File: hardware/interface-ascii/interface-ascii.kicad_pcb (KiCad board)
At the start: 2 copper layers, 88.9 x 132.1 mm, 49 parts, among them J1 Apple 2, J2 Apple 1, J3 UART, J4 Conn_01x05, J5 ISP header, J6 Keyboard, J7 SOL-20, SW1 Options, U1 ATmega328P, U2 74LS166, U3 74LS138, U4 74LS138, U5 74LS04

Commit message: Move i/o and serial connectors to edge of PCB
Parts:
- moved J3 14.2 mm to (242.6, 61.5)
- moved J4 13.0 mm to (166.9, 61.6)
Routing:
- net +5V: track 586.0 -> 568.2 mm
- net GND: track 459.3 -> 476.2 mm, vias 3 -> 4
- net /Rx: track 130.2 -> 145.1 mm
- net /OUT1: track 96.7 -> 108.3 mm
- net /OUT3: track 190.1 -> 201.5 mm
- net /Tx: track 128.6 -> 137.0 mm
- net /OUT2: track 89.0 -> 97.3 mm

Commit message: Add additional mounting holes to ASCII interface PCBS and Sol-20 PCB
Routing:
- net /OUT1: track 108.3 -> 103.1 mm
- net /Tx: track 137.0 -> 138.3 mm
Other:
- outline, holes or cut-outs redrawn
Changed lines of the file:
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@@
   (general
     (thickness 1.6)
-    (drawings 34)
+    (drawings 36)
     (tracks 1126)
     (zones 0)
@@
     )
   )
+  (gr_circle (center 174.2224 76.5048) (end 175.8099 76.5048) (layer Edge.Cuts) (width 0.1))
+  (gr_circle (center 242.6754 76.5048) (end 244.2629 76.5048) (layer Edge.Cuts) (width 0.1))
   (gr_text D17-24 (at 206.352 127.408 90) (layer F.SilkS)
     (effects (font (size 1.016 1.016) (thickness 0.1524)))
@@
   (segment (start 181.079 113.057) (end 177.396 116.74) (width 0.254) (layer B.Cu) (net 43))
   (segment (start 186.159 113.057) (end 181.079 113.057) (width 0.254) (layer B.Cu) (net 43))
-  (segment (start 245.214 61.52548) (end 245.16828 61.47976) (width 0.254) (layer B.Cu) (net 44))
-  (segment (start 244.706 83.466) (end 245.214 82.958) (width 0.254) (layer B.Cu) (net 44))
-  (segment (start 245.214 64.543) (end 245.214 61.52548) (width 0.254) (layer B.Cu) (net 44))
-  (segment (start 245.214 82.958) (end 245.214 64.543) (width 0.254) (layer B.Cu) (net 44))
   (segment (start 211.972468 64.5938) (end 245.1632 64.5938) (width 0.254) (layer B.Cu) (net 44))
   (segment (start 211.969398 64.59073) (end 211.972468 64.5938) (width 0.254) (layer B.Cu) (net 44))
@@
   (segment (start 190.111999 111.929999) (end 188.715001 111.929999) (width 0.254) (layer B.Cu) (net 44))
   (segment (start 191.239 113.057) (end 190.111999 111.929999) (width 0.254) (layer B.Cu) (net 44))
+  (segment (start 245.214 64.543) (end 245.214 61.52548) (width 0.254) (layer B.Cu) (net 44))
+  (segment (start 246.7888 66.1178) (end 245.214 64.543) (width 0.254) (layer B.Cu) (net 44))
+  (segment (start 245.214 61.52548) (end 245.16828 61.47976) (width 0.254) (layer B.Cu) (net 44))
+  (segment (start 246.7888 81.3832) (end 246.7888 66.1178) (width 0.254) (layer B.Cu) (net 44))
+  (segment (start 244.706 83.466) (end 246.7888 81.3832) (width 0.254) (layer B.Cu) (net 44))
   (segment (start 188.6228 113.1332) (end 188.699 113.057) (width 0.254) (layer B.Cu) (net 45))
   (segment (start 188.699 113.184) (end 188.699 113.057) (width 0.254) (layer B.Cu) (net 45))
@@
   (segment (start 219.410778 63.422222) (end 200.877944 63.422222) (width 0.254) (layer B.Cu) (net 86))
   (segment (start 195.350165 68.950001) (end 194.550166 69.75) (width 0.254) (layer B.Cu) (net 86))
-  (segment (start 174.475 71.909) (end 174.475 61.622) (width 0.254) (layer B.Cu) (net 86))
-  (segment (start 174.475 74.576) (end 174.475 71.909) (width 0.254) (layer B.Cu) (net 86))
-  (segment (start 179.682 79.783) (end 174.475 74.576) (width 0.254) (layer B.Cu) (net 86))
-  (segment (start 179.682 82.323) (end 179.682 79.783) (width 0.254) (layer B.Cu) (net 86))
-  (segment (start 192.416566 71.8836) (end 174.5004 71.8836) (width 0.254) (layer B.Cu) (net 86))
+  (segment (start 176.7102 63.8572) (end 174.475 61.622) (width 0.254) (layer B.Cu) (net 86))
+  (segment (start 179.682 66.8544) (end 176.7356 63.908) (width 0.254) (layer B.Cu) (net 86))
+  (segment (start 179.682 82.323) (end 179.682 66.8544) (width 0.254) (layer B.Cu) (net 86))
+  (segment (start 192.416566 71.8836) (end 179.682 71.8836) (width 0.254) (layer B.Cu) (net 86))
   (segment (start 194.550166 69.75) (end 192.416566 71.8836) (width 0.254) (layer B.Cu) (net 86))
   (segment (start 188.713407 85.864593) (end 187.937 86.641) (width 0.254) (layer F.Cu) (net 87))
@@
   (segment (start 196.558593 85.864593) (end 188.713407 85.864593) (width 0.254) (layer F.Cu) (net 87))
   (segment (start 197.97 87.276) (end 196.558593 85.864593) (width 0.254) (layer F.Cu) (net 87))
-  (segment (start 178.666 81.307) (end 178.666 83.593) (width 0.254) (layer B.Cu) (net 87))
-  (segment (start 171.935 74.576) (end 178.666 81.307) (width 0.254) (layer B.Cu) (net 87))
   (segment (start 179.072399 83.999399) (end 178.666 83.593) (width 0.254) (layer F.Cu) (net 87))
   (segment (start 181.714 86.641) (end 179.072399 83.999399) (width 0.254) (layer F.Cu) (net 87))
   (via (at 178.666 83.593) (size 0.8128) (drill 0.4064) (layers F.Cu B.Cu) (net 87))
   (segment (start 197.97 87.276) (end 197.97 87.3395) (width 0.254) (layer B.Cu) (net 87))
-  (segment (start 171.935 74.576) (end 171.935 61.622) (width 0.254) (layer B.Cu) (net 87))
   (segment (start 171.935 60.419919) (end 173.730119 58.6248) (width 0.254) (layer B.Cu) (net 87))
   (segment (start 219.2298 58.6248) (end 220.4998 59.8948) (width 0.254) (layer B.Cu) (net 87))
   (segment (start 171.935 61.622) (end 171.935 60.419919) (width 0.254) (layer B.Cu) (net 87))
   (segment (start 173.730119 58.6248) (end 219.2298 58.6248) (width 0.254) (layer B.Cu) (net 87))
+  (segment (start 178.666 68.3276) (end 178.666 83.593) (width 0.254) (layer B.Cu) (net 87))
+  (segment (start 171.9604 61.622) (end 178.666 68.3276) (width 0.254) (layer B.Cu) (net 87))
+  (segment (start 171.935 61.622) (end 171.9604 61.622) (width 0.254) (layer B.Cu) (net 87))
   (segment (start 184.254 77.497) (end 184.381 77.497) (width 0.254) (layer B.Cu) (net 88))
   (segment (start 209.146 113.057) (end 209.019 113.184) (width 0.254) (layer B.Cu) (net 88))

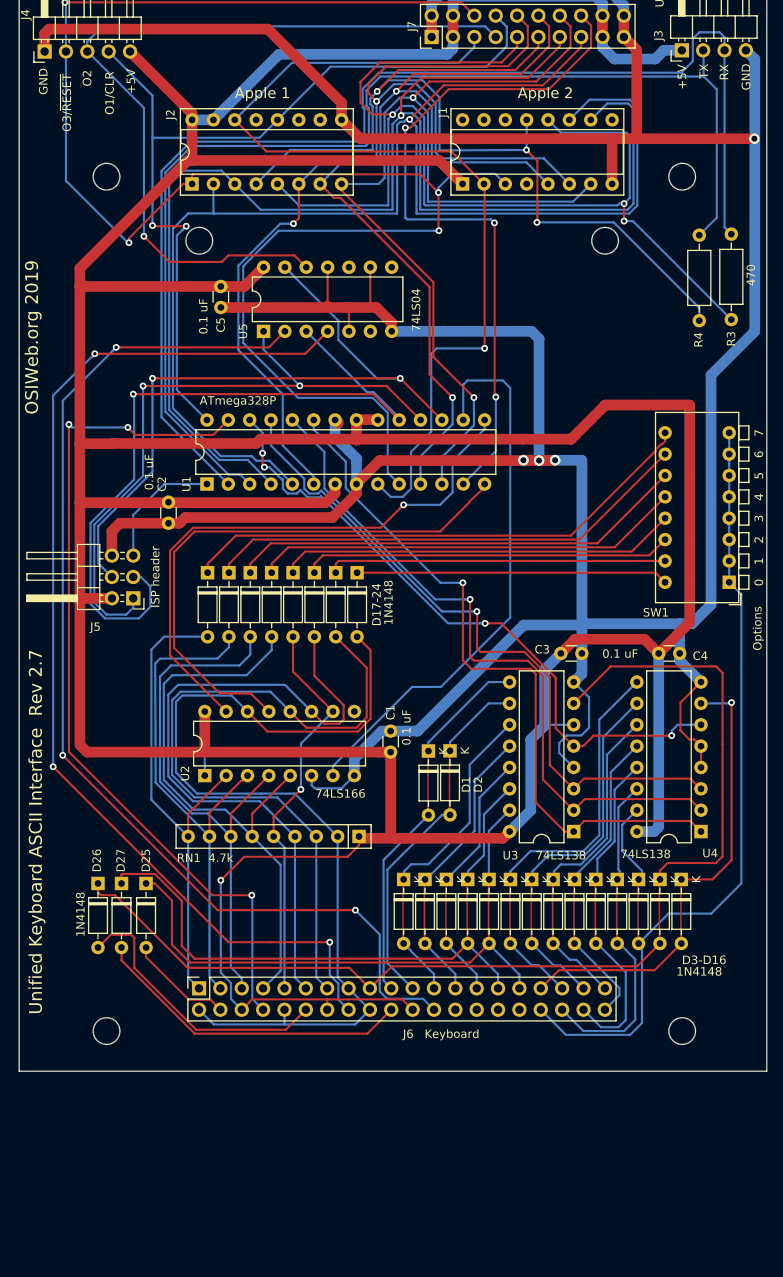
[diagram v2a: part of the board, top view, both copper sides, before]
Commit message: mechanical fit and buildability fixes
- Moved header slightly forward

- Moved interface mount holes do reduce interference with case mount holes

- For all keys in classic keyboard, add option for either through-hole or SMT
diodes and resistors.
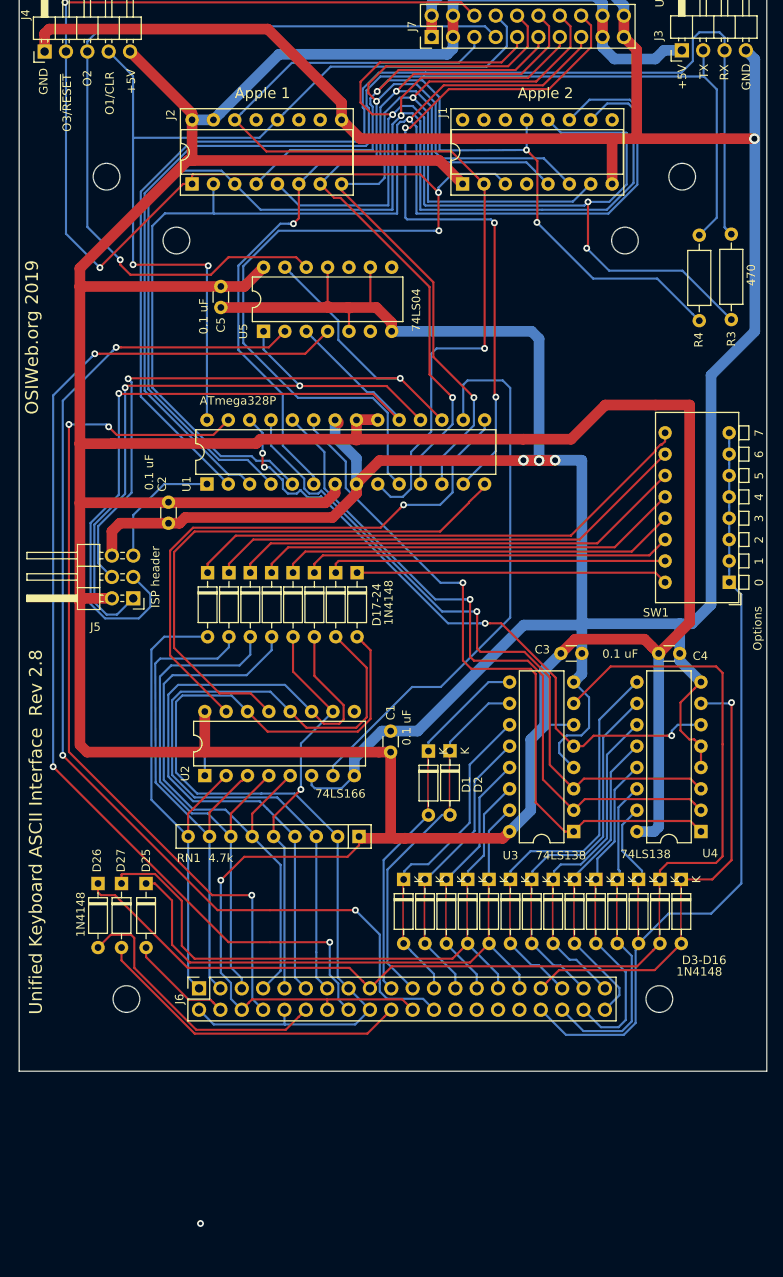
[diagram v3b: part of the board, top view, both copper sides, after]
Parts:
- J6: footprint unikbd:PinHeader_2x20_P2.54mm_Vertical -> unikbd:kbd_header_and_mounting_holes
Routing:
- net /OUT3: track 201.5 -> 207.4 mm
- net /D0: track 131.1 -> 136.3 mm
- net /OUT2: track 97.3 -> 102.0 mm
- net /OUT1: track 103.1 -> 107.5 mm
- net /D3: track 167.0 -> 169.2 mm
- net /Tx: track 138.3 -> 140.3 mm
- net /Rx: track 145.1 -> 147.2 mm
- net /MOSI-OUT2: track 84.0 -> 86.0 mm
- net /D1: track 108.7 -> 107.9 mm
- net /D2: track 165.1 -> 165.7 mm
- net /Row12: track 8.74 -> 8.22 mm
- net (no net): vias 0 -> 1
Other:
- outline, holes or cut-outs redrawn
- board text added: "Unified Keyboard ASCII Interface Rev 2.8"
- board text removed: "Mounting holes: 0.125" Non-plated 2.5" square spacing Pin 1 of connector 0.31", 0" (x,y) relative to center of left lower hole."
- board text removed: "Pin 1 of keyboard connector must be at least 3.5" from pin 1 of interface connector in order for interface connector to be accessible with keyboard assembled."
- board text removed: "Unified Keyboard ASCII Interface Rev 2.7"

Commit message: Add BOM parameter fields to apple2 and 328P encoders and classic kbd
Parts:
- J4: value Conn_01x05 -> Outputs

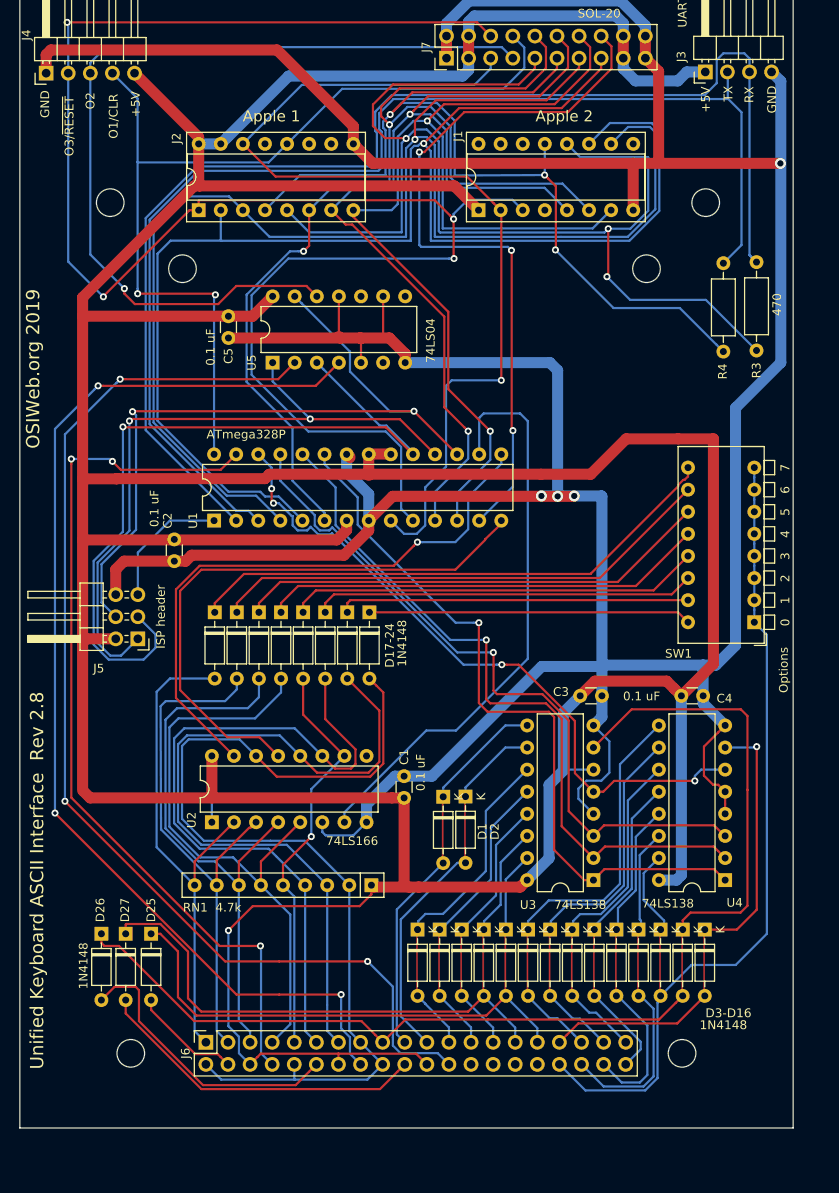
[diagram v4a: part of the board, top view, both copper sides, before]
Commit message: Removed vestigial R4 resistor and moved R3 to be on RX line.
Now, R3 only needs to be installed when using the serial port.  A zero-ohm
jumper can be used for serial-only output.
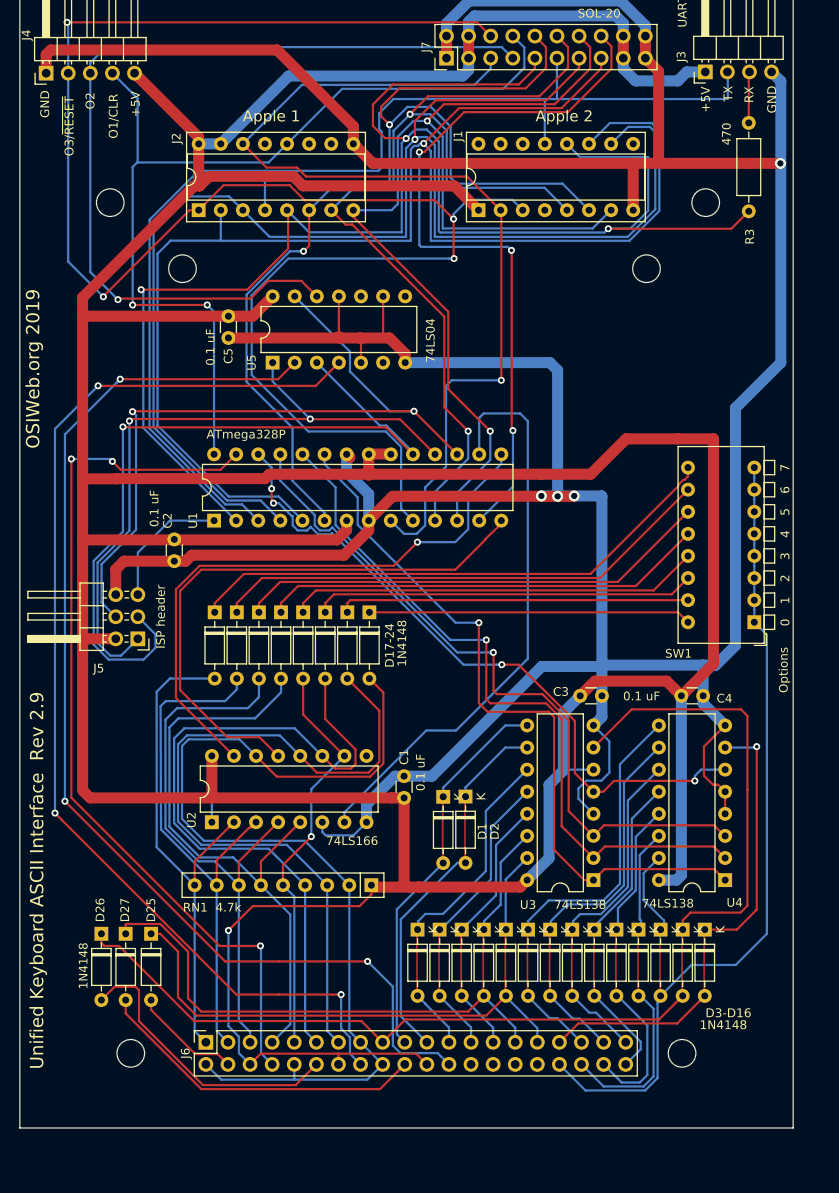
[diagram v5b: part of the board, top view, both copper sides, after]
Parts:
- removed the R3 at (248.5, 93.5)
- moved R3 16.4 mm to (247.6, 77.5)
- renumbered R4 to R3
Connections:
- J3 pad 2: /Tx -> /D1
- R3 pad 1: /D1 -> /D0
- R3 pad 2: /Tx -> /Rx
- U1 pad 2: /Rx -> /D0
- U1 pad 3: /Tx -> /D1
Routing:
- net /Rx: track 147.2 -> 5.89 mm
- net /Tx: track 140.3 -> 0.00 mm
- net /D0: track 136.3 -> 181.4 mm
- net /D1: track 107.9 -> 134.6 mm, vias 3 -> 0
- net +5V: track 568.2 -> 569.1 mm
- net /OUT2: track 102.0 -> 102.9 mm
- net /OUT3: track 207.4 -> 208.2 mm
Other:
- board text added: "Unified Keyboard ASCII Interface Rev 2.9"
- board text removed: "Unified Keyboard ASCII Interface Rev 2.8"

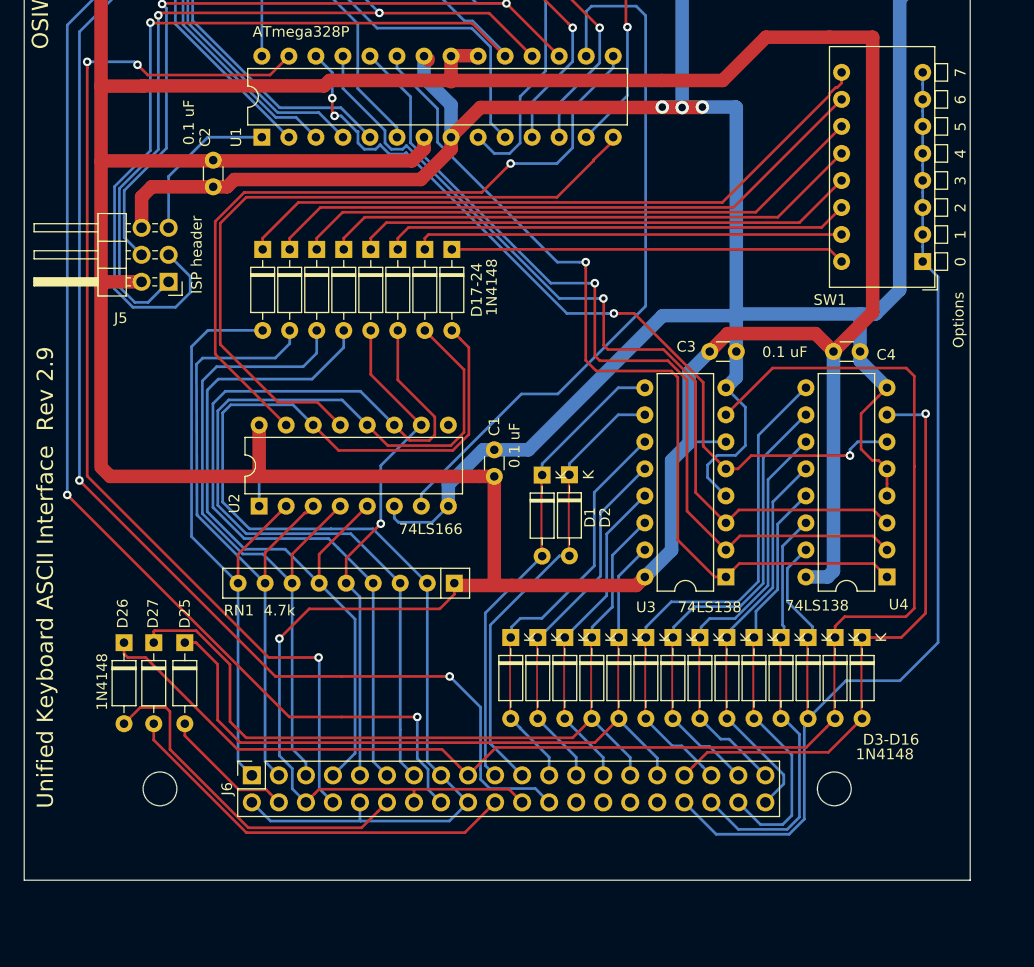
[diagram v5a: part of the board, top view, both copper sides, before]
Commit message: Update interface-ascii to use either DIP switch or header-jumper
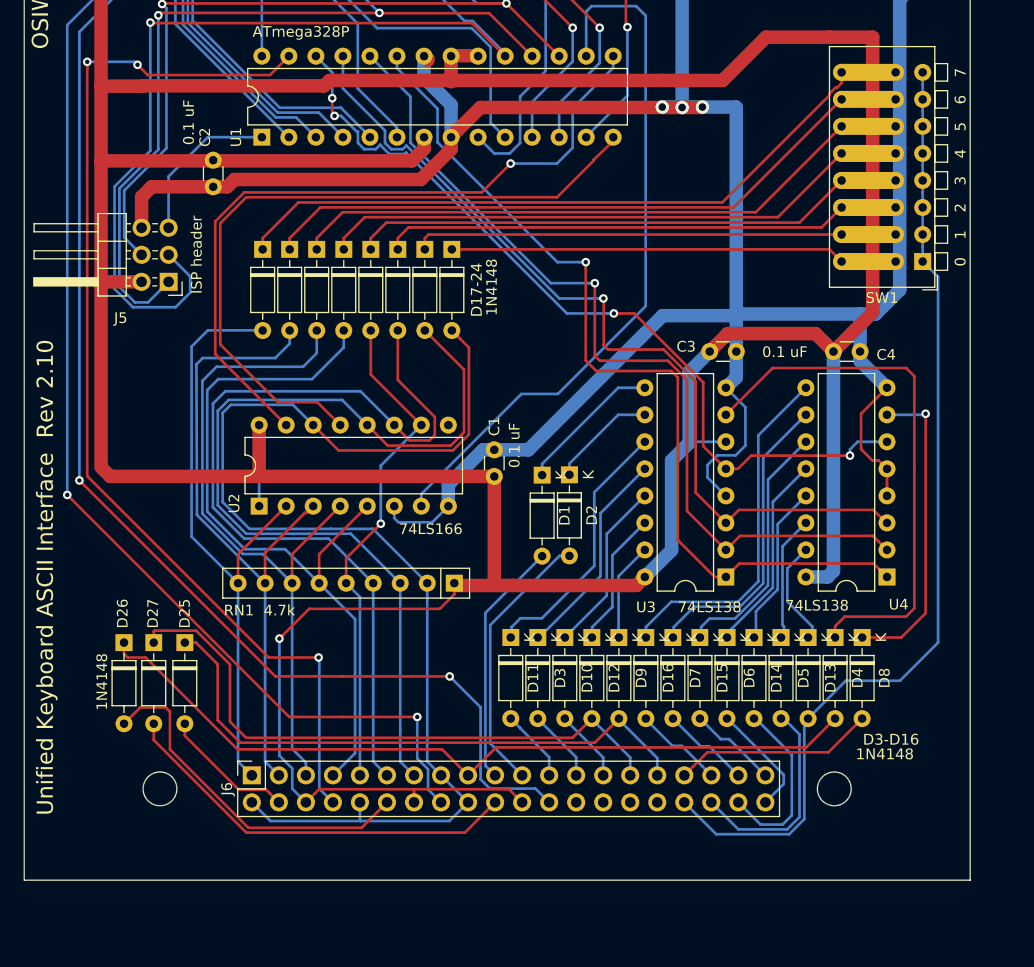
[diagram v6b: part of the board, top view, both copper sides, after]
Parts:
- D1, D10, D11, D12, D13, D14, D15, D16, D2, D3, D4, D5, D6, D7, D8, D9: footprint unikbd:D_DO-35_SOD27_P7.62mm_Horizontal_bypassed -> Diode_THT:D_DO-35_SOD27_P7.62mm_Horizontal
- SW1: footprint Button_Switch_THT:SW_DIP_SPSTx08_Piano_CTS_Series194-8MSTN_W7.62mm_P2.54mm -> unikbd:SW_DIP_SPSTx08_Piano_CTS_Series194-8MSTN_W7.62mm_P2.54mm
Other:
- board text added: "Unified Keyboard ASCII Interface Rev 2.10"
- board text removed: "Unified Keyboard ASCII Interface Rev 2.9"
